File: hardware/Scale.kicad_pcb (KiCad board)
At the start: 2 copper layers, 58.2 x 25.9 mm, 45 parts, among them J1 Load Cell Connector, J2 DebugEdge_02x03, J3 Display Connector, J4 GPIO, J5 RS232, J6 USB_C_Receptacle, Q1 DMG2307L, Q2 DMG2307L, Q3 BSD235N, SW1 RESET, SW2 PEC12R Encoder, U1 STM32G070CBTx_u, U3 MCP6N11-010, U4 MCP4542, U5 AP9101CK, U6 MIC5504-3.3YM5, X1 KC2520Z

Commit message: Started on pcb
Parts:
- removed the C4 at (117.2, 60.7)
- removed J6: USB_C_Receptacle, Custom:USB_C_Receptacle_Amphenol_12401610E4-2A
- removed SW2: PEC12R Encoder, Custom:Bourns PEC12R Vertical
- added C10: 1uF, Capacitor_SMD:C_0603_1608Metric, F.Cu at (150.0, 63.8)
- added C12: 1uF, Capacitor_SMD:C_0603_1608Metric, F.Cu at (144.7, 66.0)
- added C13: 1uF, Capacitor_SMD:C_0603_1608Metric, F.Cu at (144.7, 64.5)
- added C14: 1uF, Capacitor_SMD:C_0603_1608Metric, F.Cu at (141.6, 66.0)
- added C15: 220nF, Capacitor_SMD:C_0603_1608Metric, F.Cu at (147.8, 67.5)
- added C16: 47nF, Capacitor_SMD:C_0603_1608Metric, F.Cu at (147.8, 70.6)
- added C18: 10uF, Capacitor_SMD:C_1210_3225Metric, F.Cu at (131.6, 58.8)
- added C19: 10uF, Capacitor_SMD:C_1210_3225Metric, F.Cu at (136.3, 56.0)
- added C23: 100nF, Capacitor_SMD:C_0603_1608Metric, F.Cu at (141.8, 69.6)
- added C27: 100nF, Capacitor_SMD:C_0603_1608Metric, F.Cu at (155.1, 47.7)
- added C28: 100nF, Capacitor_SMD:C_0603_1608Metric, F.Cu at (155.1, 49.2)
- added C29: 10uF, Capacitor_SMD:C_0603_1608Metric, F.Cu at (152.8, 48.4)
- added C30: 100nF, Capacitor_SMD:C_0603_1608Metric, F.Cu at (156.6, 59.1)
- added C31: 100nF, Capacitor_SMD:C_0603_1608Metric, F.Cu at (156.7, 60.6)
- added C5: 100nF, Capacitor_SMD:C_0603_1608Metric, F.Cu at (137.2, 69.5)
- added C6: 10nF, Capacitor_SMD:C_0603_1608Metric, F.Cu at (149.5, 53.9)
- added C7: 100nF, Capacitor_SMD:C_0603_1608Metric, F.Cu at (146.2, 51.9)
- added C8: 10nF, Capacitor_SMD:C_0603_1608Metric, F.Cu at (143.0, 53.9)
- added C9: 100nF, Capacitor_SMD:C_0603_1608Metric, F.Cu at (140.3, 69.6)
- added J7: 12401610E4#2A, custom:12401610E42A, F.Cu at (118.3, 52.9)
- added L1: 10uH, Inductor_SMD:L_1210_3225Metric, F.Cu at (139.7, 56.0)
- added R1: 1.0K 1%, Resistor_SMD:R_0603_1608Metric, F.Cu at (68.7, 48.3)
- added R10: 20k 1%, Resistor_SMD:R_0603_1608Metric, F.Cu at (143.8, 51.6)
- added R11: 20k 1%, Resistor_SMD:R_0603_1608Metric, F.Cu at (141.6, 64.5)
- added R13: 20k 1%, Resistor_SMD:R_0603_1608Metric, F.Cu at (147.0, 63.7)
- added R16: 20k 1%, Resistor_SMD:R_0603_1608Metric, F.Cu at (148.5, 63.8)
- added R17: 10k 1%, Resistor_SMD:R_0603_1608Metric, F.Cu at (147.8, 66.0)
- added R18: 20k 1%, Resistor_SMD:R_0603_1608Metric, F.Cu at (147.8, 69.1)
- added R2: 1.0K 1%, Resistor_SMD:R_0603_1608Metric, F.Cu at (68.7, 50.8)
- added R27: 1K, Resistor_SMD:R_0603_1608Metric, F.Cu at (68.7, 63.4)
- added R28: 1K, Resistor_SMD:R_0603_1608Metric, F.Cu at (68.7, 65.9)
- added R29: 1K, Resistor_SMD:R_0603_1608Metric, F.Cu at (68.7, 68.4)
- added R3: 1.0K 1%, Resistor_SMD:R_0603_1608Metric, F.Cu at (68.7, 53.3)
- added R36: 10R 1%, Resistor_SMD:R_0603_1608Metric, F.Cu at (157.3, 48.4)
- added R37: 10R 1%, Resistor_SMD:R_0603_1608Metric, F.Cu at (157.4, 62.8)
- added R38: 10R 1%, Resistor_SMD:R_0603_1608Metric, F.Cu at (155.9, 67.2)
- added R39: 10R 1%, Resistor_SMD:R_0603_1608Metric, F.Cu at (154.4, 67.2)
- added R4: 1.0K 1%, Resistor_SMD:R_0603_1608Metric, F.Cu at (68.7, 55.9)
- added R40: 10R 1%, Resistor_SMD:R_0603_1608Metric, F.Cu at (152.9, 67.2)
- added R41: 10R 1%, Resistor_SMD:R_0603_1608Metric, F.Cu at (151.4, 67.2)
- added R42: 10R 1%, Resistor_SMD:R_0603_1608Metric, F.Cu at (155.9, 62.9)
- added R43: 10R 1%, Resistor_SMD:R_0603_1608Metric, F.Cu at (154.4, 62.8)
- added R44: 10K 1%, Resistor_SMD:R_0603_1608Metric, F.Cu at (156.7, 65.0)
- added R5: 1.0K 1%, Resistor_SMD:R_0603_1608Metric, F.Cu at (68.7, 58.4)
- added R6: 1.0K 1%, Resistor_SMD:R_0603_1608Metric, F.Cu at (68.7, 60.9)
- added R7: 100k 1%, Resistor_SMD:R_0603_1608Metric, F.Cu at (138.2, 67.2)
- added R8: 100k 1%, Resistor_SMD:R_0603_1608Metric, F.Cu at (138.7, 69.5)
- added R9: 20k 1%, Resistor_SMD:R_0603_1608Metric, F.Cu at (148.8, 51.6)
- added S1: PEC12R-3217F-S0024, custom:PEC12R3217FS0024, F.Cu at (151.7, 89.7)
- added TP1: TP_INA_OUT_UNFILTERED, TestPoint:TestPoint_Pad_D1.5mm, B.Cu at (72.5, 48.8)
- added TP2: TP_ADC_VREF, TestPoint:TestPoint_Pad_D1.5mm, B.Cu at (72.5, 52.4)
- added TP3: TP_INA_OUT_ACTIVE, TestPoint:TestPoint_Pad_D1.5mm, B.Cu at (72.5, 55.9)
- added TP4: TP_INA_OUT_FILTERED_PASSIVE, TestPoint:TestPoint_Pad_D1.5mm, B.Cu at (72.5, 59.5)
- added TP5: TP_INA_IN_P, TestPoint:TestPoint_Pad_D1.5mm, B.Cu at (76.1, 48.8)
- added TP6: TP_INA_IN_N, TestPoint:TestPoint_Pad_D1.5mm, B.Cu at (76.1, 52.4)
- added TP_3V1: TP_3V3, TestPoint:TestPoint_Pad_D1.5mm, B.Cu at (76.1, 55.9)
- added TP_3V3A1: TP_3V3A, TestPoint:TestPoint_Pad_D1.5mm, B.Cu at (76.1, 59.5)
- added TP_BAT_N1: TP_BAT_N, TestPoint:TestPoint_Pad_D1.5mm, B.Cu at (79.6, 48.8)
- added TP_GND1: TP_GND, TestPoint:TestPoint_Pad_D1.5mm, B.Cu at (79.6, 52.4)
- added TP_VDD1: TP_VDD, TestPoint:TestPoint_Pad_D1.5mm, B.Cu at (79.6, 55.9)
- added U10: MCP6001-OT, Package_TO_SOT_SMD:SOT-23-5, F.Cu at (138.2, 64.3)
- added U2: MCP3562R-E/ST, Package_SO:TSSOP-20_4.4x6.5mm_P0.65mm, F.Cu at (154.7, 54.5)
- added U9: MCP6001-OT, Package_TO_SOT_SMD:SOT-23-5, F.Cu at (144.4, 69.0)
- C1, C2, C3: footprint Capacitor_SMD:C_0603_1608Metric_Pad1.08x0.95mm_HandSolder -> Capacitor_SMD:C_0603_1608Metric
- C11: renamed from C6; footprint Capacitor_SMD:C_0603_1608Metric_Pad1.08x0.95mm_HandSolder -> Capacitor_SMD:C_0603_1608Metric
- C17: renamed from C7; footprint Capacitor_SMD:C_0603_1608Metric_Pad1.08x0.95mm_HandSolder -> Capacitor_SMD:C_0603_1608Metric
- C4: renamed from C5; footprint Capacitor_SMD:C_0603_1608Metric_Pad1.08x0.95mm_HandSolder -> Capacitor_SMD:C_0603_1608Metric
- D1: footprint Diode_SMD:D_SOD-323_HandSoldering -> Diode_SMD:D_SOD-323F
- J4: renamed from J2; footprint custom:DebugEdge_2x03_Target -> Connector_DebugEdge:DebugEdge_2x03_Target
- J5: renamed from J3; footprint Custom:0.96'' Display -> Connector_PinHeader_2.54mm:PinHeader_1x04_P2.54mm_Vertical
- R12: renamed from R1; footprint Resistor_SMD:R_0603_1608Metric_Pad0.98x0.95mm_HandSolder -> Resistor_SMD:R_0603_1608Metric
- R14: renamed from R2; footprint Resistor_SMD:R_0603_1608Metric_Pad0.98x0.95mm_HandSolder -> Resistor_SMD:R_0603_1608Metric
- R15: renamed from R3; footprint Resistor_SMD:R_0603_1608Metric_Pad0.98x0.95mm_HandSolder -> Resistor_SMD:R_0603_1608Metric
- R19: renamed from R9; footprint Resistor_SMD:R_0603_1608Metric_Pad0.98x0.95mm_HandSolder -> Resistor_SMD:R_0603_1608Metric
- R20: renamed from R10; footprint Resistor_SMD:R_0603_1608Metric_Pad0.98x0.95mm_HandSolder -> Resistor_SMD:R_0603_1608Metric
- R21: renamed from R11; footprint Resistor_SMD:R_0603_1608Metric_Pad0.98x0.95mm_HandSolder -> Resistor_SMD:R_0603_1608Metric
- R22: renamed from R12; footprint Resistor_SMD:R_0603_1608Metric_Pad0.98x0.95mm_HandSolder -> Resistor_SMD:R_0603_1608Metric
- R23: renamed from R13; footprint Resistor_SMD:R_0603_1608Metric_Pad0.98x0.95mm_HandSolder -> Resistor_SMD:R_0603_1608Metric
- R24: renamed from R14; footprint Resistor_SMD:R_0603_1608Metric_Pad0.98x0.95mm_HandSolder -> Resistor_SMD:R_0603_1608Metric
- R25: renamed from R15; footprint Resistor_SMD:R_0603_1608Metric_Pad0.98x0.95mm_HandSolder -> Resistor_SMD:R_0603_1608Metric
- R26: renamed from R16; footprint Resistor_SMD:R_0603_1608Metric_Pad0.98x0.95mm_HandSolder -> Resistor_SMD:R_0603_1608Metric
- moved J3 45.5 mm to (114.6, 90.2), turned to 90 degrees
- moved R33 40.5 mm to (135.0, 87.3), turned to 180 degrees
- moved C21 38.5 mm to (135.0, 85.8), turned to 0 degrees
- moved R22 20.5 mm to (129.0, 85.9)
- moved Q1 20.1 mm to (131.5, 86.4), turned to -90 degrees
- moved J5 19.5 mm to (129.8, 90.2), turned to -90 degrees
- moved R32 19.2 mm to (138.1, 84.3)
- moved C20 19.2 mm to (138.1, 79.7)
- moved R30 19.2 mm to (138.1, 81.3)
- moved R31 19.2 mm to (138.1, 82.8)
- moved C22 19.2 mm to (138.1, 87.3)
- moved R34 19.2 mm to (138.1, 85.8)
- moved C11 19.0 mm to (150.0, 60.8), turned to 90 degrees
- moved R19 18.4 mm to (127.5, 85.9), turned to 90 degrees
- moved J4 16.8 mm to (113.2, 63.6)
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- renumbered C8 to C20, C10 to C21, C9 to C22, J4 to J2, J5 to J3, R4 to R30, R5 to R31, R6 to R32, R7 to R33, R8 to R34, U5 to U7, U6 to U8
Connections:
- net /I2C_SCL renamed /Display/SCL
- net /I2C_SDA renamed /Display/SDA
- net /Instrumentation Amplifier/INA_OUT renamed /Instrumentation Amplifier/INA_OUT_UNFILTERED
- C11 pad 1: +3V3 -> +3.3VA
- C3 pad 1: /MCU/MCU_VREF -> +3.3VA
- D1 pad 1: /Instrumentation Amplifier/BRIDGE_B -> /Instrumentation Amplifier/INA_IN_P
- D1 pad 2: /Instrumentation Amplifier/BRIDGE_A -> /Instrumentation Amplifier/INA_IN_N
- J2 pad 1: /MCU/GPIO_PA5 -> /MCU/GPIO_PB7
- Q2 pad 2: +3V3 -> +3.3VA
- R23 pad 1: +3V3 -> +3.3VA
- R25 pad 1: +BATT -> /MCU/LDO_EN
- R25 pad 2: Net-(R15-Pad2) -> GND
- U1 pad 1: unconnected-(U1-Pad1) -> /ADC/ADC_IRQ
- U1 pad 11: /Encoder/ENCODER_BUTTON -> /ADC/ADC_VREF
- U1 pad 13: /MCU/DISPLAY_ENABLE -> /Instrumentation Amplifier/INA_OUT_FILTERED_PASSIVE
- U1 pad 14: /MCU/BRIDGE_ENABLE -> /ADC/INA_OUT_FILTERED_ACTIVE
- U1 pad 15: /Instrumentation Amplifier/DPOT_HVC_A0 -> unconnected-(U1A-PA4/ADC1_IN4/I2S1_WS/RTC_OUT_ALARM/RTC_OUT_CALIB/SPI1_NSS/SPI2_MOSI/TIM14_CH1-Pad15)
- U1 pad 16: /MCU/GPIO_PA5 -> /Encoder/ENCODER_BUTTON
- U1 pad 22: unconnected-(U1-Pad22) -> /MCU/DISPLAY_ENABLE
- U1 pad 23: unconnected-(U1-Pad23) -> /MCU/BRIDGE_ENABLE
- U1 pad 24: unconnected-(U1-Pad24) -> /ADC/~{SS}
- U1 pad 25: unconnected-(U1-Pad25) -> /ADC/CLK
- U1 pad 26: unconnected-(U1-Pad26) -> /ADC/MISO
- U1 pad 27: unconnected-(U1-Pad27) -> /ADC/MOSI
- U1 pad 3: unconnected-(U1-Pad3) -> /MCU/LDO_EN
- U1 pad 4: +3V3 -> +BATT
- U1 pad 40: unconnected-(U1-Pad40) -> /ADC/ADC_MCLK
- U1 pad 41: unconnected-(U1-Pad41) -> /Instrumentation Amplifier/DPOT_HVC_A0
- U1 pad 45: /MCU/USART_TX -> /MCU/GPIO_PB5
- U1 pad 46: /MCU/USART_RX -> /MCU/GPIO_PB7
- U1 pad 47: unconnected-(U1-Pad47) -> /MCU/USART_TX
- U1 pad 48: unconnected-(U1-Pad48) -> /MCU/USART_RX
- U1 pad 5: /MCU/MCU_VREF -> +3.3VA
- U3 pad 2: /Instrumentation Amplifier/BRIDGE_A -> /Instrumentation Amplifier/INA_IN_N
- U3 pad 3: /Instrumentation Amplifier/BRIDGE_B -> /Instrumentation Amplifier/INA_IN_P
- U3 pad 5: GND -> /Instrumentation Amplifier/INA_VREF
- U3 pad 7: +3V3 -> +3.3VA
- U4 pad 5: GND -> /Instrumentation Amplifier/INA_VREF
- U8 pad 3: Net-(R15-Pad2) -> /MCU/LDO_EN
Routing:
- net +3V3: track 102.3 -> 13.8 mm, vias 2 -> 0
- net /MCU/SWDIO: track 33.7 -> 0.00 mm, vias 2 -> 0
- net +3.3VA: track 0.00 -> 33.7 mm
- net /MCU/SWDCLK: track 33.3 -> 0.00 mm, vias 3 -> 0
- net /MCU/GPIO_PA8: track 30.4 -> 0.00 mm, vias 2 -> 0
- net /Encoder/ENCODER_BUTTON: track 44.6 -> 14.4 mm, vias 4 -> 0
- net /ADC/INA_OUT_FILTERED_ACTIVE: track 0.00 -> 29.8 mm
- net /Instrumentation Amplifier/INA_OUT_UNFILTERED: track 31.7 -> 5.83 mm
- net /MCU/GPIO_PA5: track 24.0 -> 0.00 mm
- net /MCU/DISPLAY_ENABLE: track 23.7 -> 0.00 mm, vias 2 -> 0
- net /MCU/USART_RTS: track 22.7 -> 0.00 mm, vias 2 -> 0
- net /MCU/GPIO_PB3: track 21.8 -> 0.00 mm, vias 1 -> 0
- net /MCU/GPIO_PB0: track 21.8 -> 0.00 mm
- net /Instrumentation Amplifier/INA_IN_P: track 0.00 -> 21.7 mm
- net /ADC/ADC_VREF: track 0.00 -> 19.9 mm
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- removed copper zone on B.Cu, net GND
- removed copper zone on F.Cu, net GND
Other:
- board size 58.2 x 25.9 mm -> 45 x 45 mm

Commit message: Added solder bridges and calculated resistor values for INA
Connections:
- U1 pad 39: unconnected-(U1D-PD1/SPI2_SCK/TIM17_CH1-Pad39) -> /ADC/ADC_MCLK
- U1 pad 40: /ADC/ADC_MCLK -> unconnected-(U1D-PD2/TIM1_CH1N/TIM3_ETR/USART3_CK/USART3_DE/USART3_RTS-Pad40)
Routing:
- net Net-(U2-SDI): track 10.3 -> 0.00 mm
- net Net-(U2-*CS): track 9.24 -> 0.00 mm
- net Net-(U2-SCK): track 8.89 -> 0.00 mm
- net /ADC/ADC_MCLK: track 6.61 -> 0.00 mm

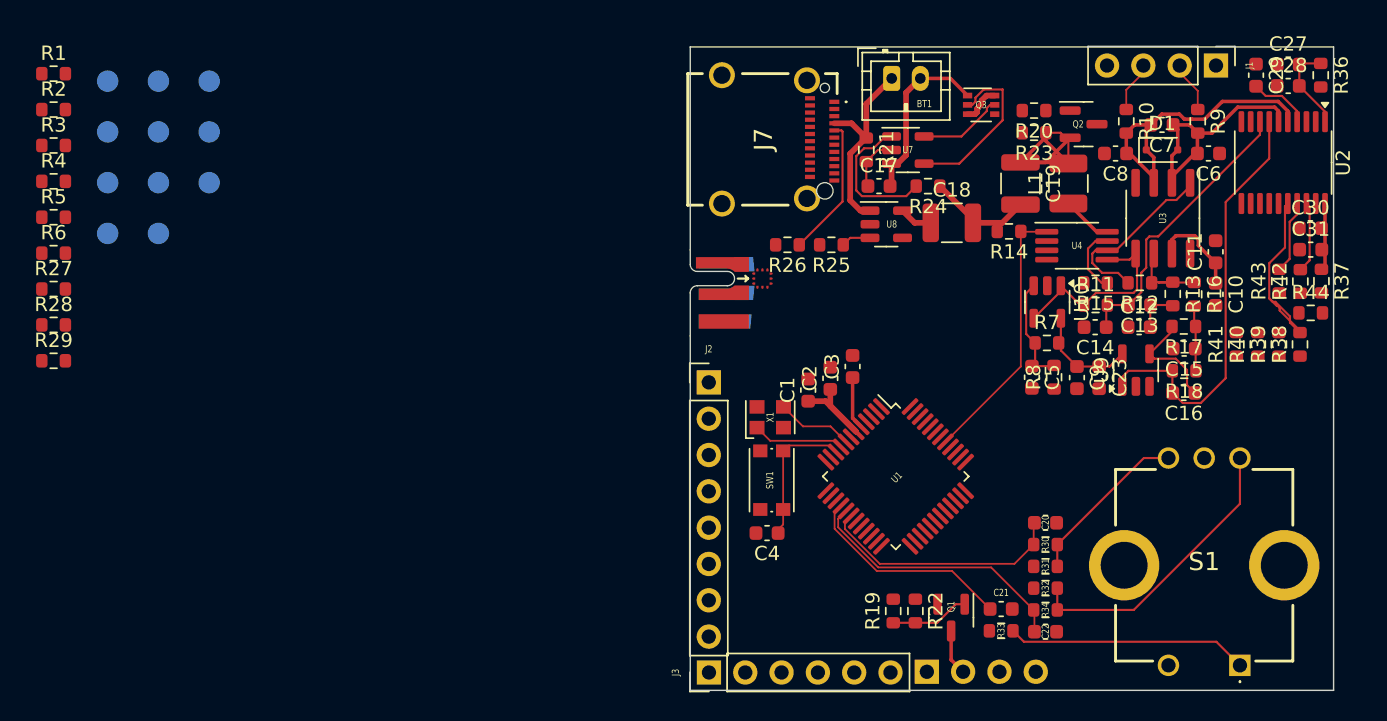
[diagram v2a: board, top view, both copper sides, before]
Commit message: Set jumper footprints and updated design rules for Oshpark After Dark
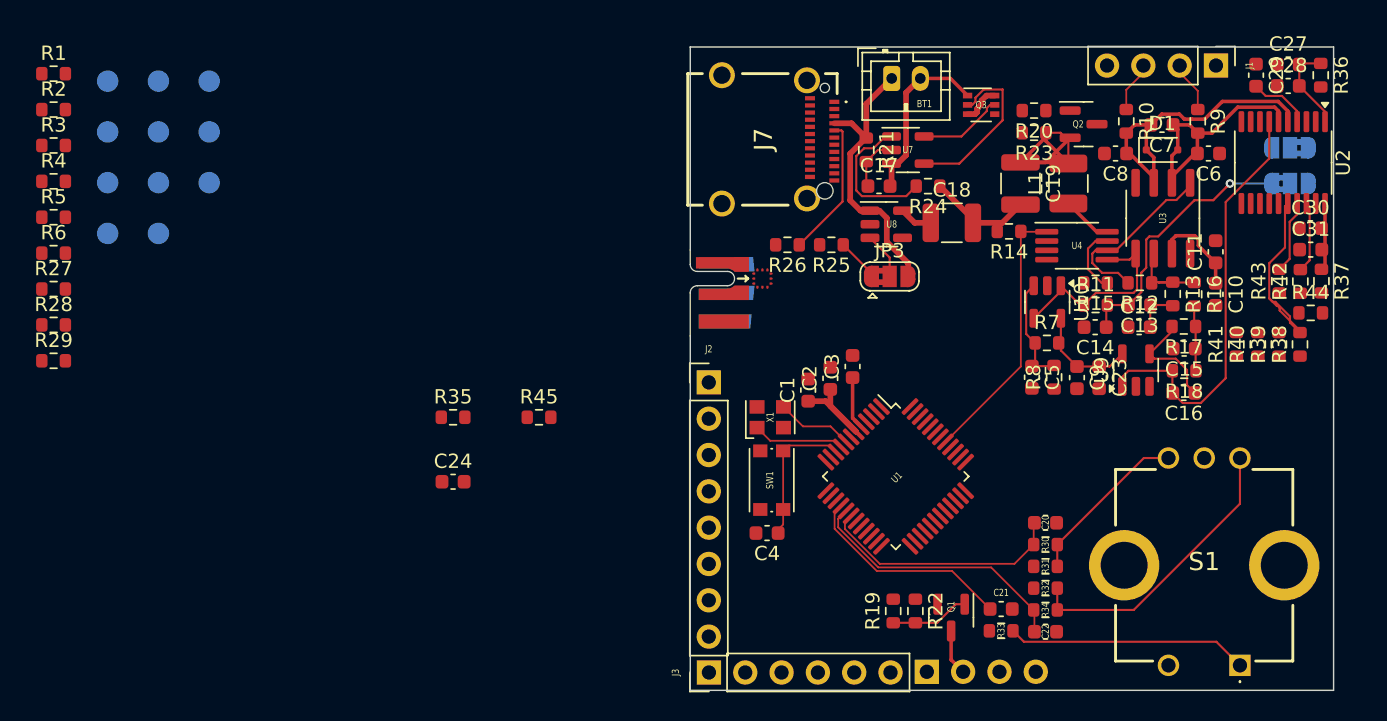
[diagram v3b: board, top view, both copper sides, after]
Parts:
- added C24: 1uF, Capacitor_SMD:C_0603_1608Metric, F.Cu at (96.7, 76.9)
- added JP1: SolderJumper_3_Bridged12, Jumper:SolderJumper-3_P1.3mm_Bridged2Bar12_RoundedPad1.0x1.5mm, B.Cu at (155.2, 56.0)
- added JP2: SolderJumper_3_Bridged12, Jumper:SolderJumper-3_P1.3mm_Bridged2Bar12_RoundedPad1.0x1.5mm, B.Cu at (155.2, 53.5)
- added JP3: SolderJumper_3_Bridged12, Jumper:SolderJumper-3_P1.3mm_Bridged2Bar12_RoundedPad1.0x1.5mm, F.Cu at (127.2, 62.5)
- added R35: 10K 1%, Resistor_SMD:R_0603_1608Metric, F.Cu at (96.7, 72.3)
- added R45: 1k 1%, Resistor_SMD:R_0603_1608Metric, F.Cu at (102.7, 72.3)
- R12: value 100k 1% -> 330k 1%
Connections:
- U2 pad 3: GND -> Net-(JP1-C)
- U2 pad 8: /ADC/ADC_VREF -> /ADC/INA_OUT_FILTERED_PASSIVE
- U4 pad 5: /Instrumentation Amplifier/INA_VREF -> Net-(U4-P0W)
- U8 pad 3: /MCU/LDO_EN -> Net-(JP3-C)
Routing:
- net +BATT: track 14.1 -> 20.2 mm
- net Net-(JP3-C): track 0.00 -> 2.97 mm
- net /ADC/ADC_VREF: track 19.9 -> 18.8 mm, vias 0 -> 1
- net /MCU/LDO_EN: track 2.08 -> 3.02 mm

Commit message: Some more routing
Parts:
- removed JP3: SolderJumper_3_Bridged12, Jumper:SolderJumper-3_P1.3mm_Bridged2Bar12_RoundedPad1.0x1.5mm
- removed R25: 100K, Resistor_SMD:R_0603_1608Metric
- moved R35 56.0 mm to (151.4, 60.8), turned to -90 degrees
- moved R45 42.7 mm to (142.5, 57.0), turned to -90 degrees
- moved C24 31.3 mm to (123.2, 60.3)
- moved R40 5.10 mm to (152.9, 72.3), turned to 180 degrees
- moved R41 3.90 mm to (152.9, 70.8), turned to 180 degrees
- turned C14 to 0 degrees
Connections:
- U1 pad 3: /MCU/LDO_EN -> unconnected-(U1C-PC15-OSC32_OUT(PC15)/RCC_OSC32_EN/RCC_OSC32_OUT/RCC_OSC_EN/TIM15_BK-Pad3)
- U1 pad 4: +BATT -> +3.3VA
- U8 pad 3: Net-(JP3-C) -> +BATT
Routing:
- net /ADC/ADC_IRQ: track 0.00 -> 38.1 mm, vias 0 -> 4
- net /MCU/BRIDGE_ENABLE: track 0.00 -> 36.1 mm
- net /ADC/~{SS}: track 0.00 -> 34.4 mm
- net /ADC/MISO: track 0.00 -> 34.3 mm
- net /ADC/ADC_MCLK: track 0.00 -> 33.3 mm, vias 0 -> 4
- net /ADC/MOSI: track 0.00 -> 32.6 mm
- net /Instrumentation Amplifier/INA_ENABLE: track 0.00 -> 32.3 mm, vias 0 -> 4
- net /ADC/CLK: track 0.00 -> 29.6 mm
- net /Instrumentation Amplifier/INA_OUT_FILTERED_PASSIVE: track 3.03 -> 31.7 mm, vias 0 -> 2
- net /ADC/INA_OUT_FILTERED_ACTIVE: track 29.8 -> 57.8 mm, vias 0 -> 2
- net /MCU/GPIO_PA8: track 0.00 -> 18.5 mm, vias 0 -> 2
- net /MCU/GPIO_PB0: track 0.00 -> 16.6 mm
- net Net-(U2-SCK): track 0.00 -> 16.2 mm
- net /MCU/GPIO_PB1: track 0.00 -> 15.3 mm
- net /Display/SDA: track 0.00 -> 14.4 mm, vias 0 -> 2
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- added copper zone on B.Cu, net GND
- added copper zone on F.Cu, net GND

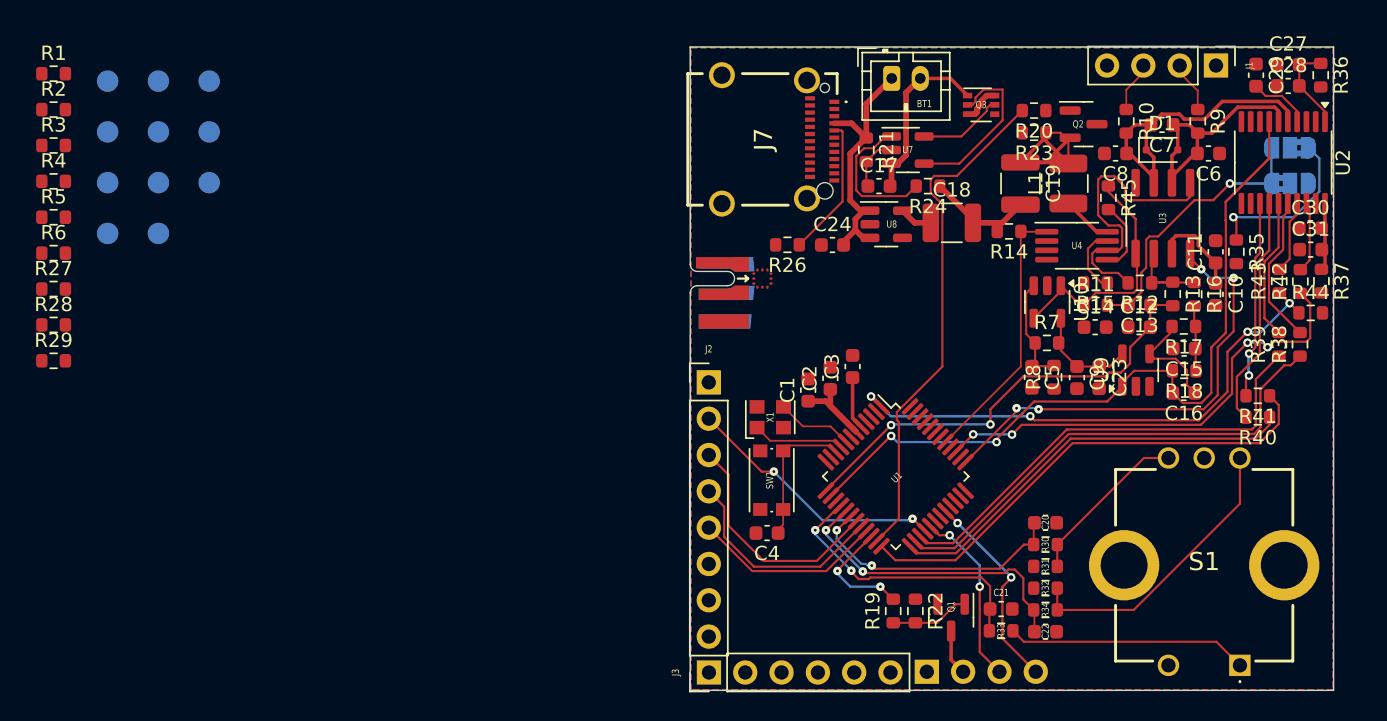
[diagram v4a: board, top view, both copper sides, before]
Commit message: Updated design rules and ran and implemented DRC
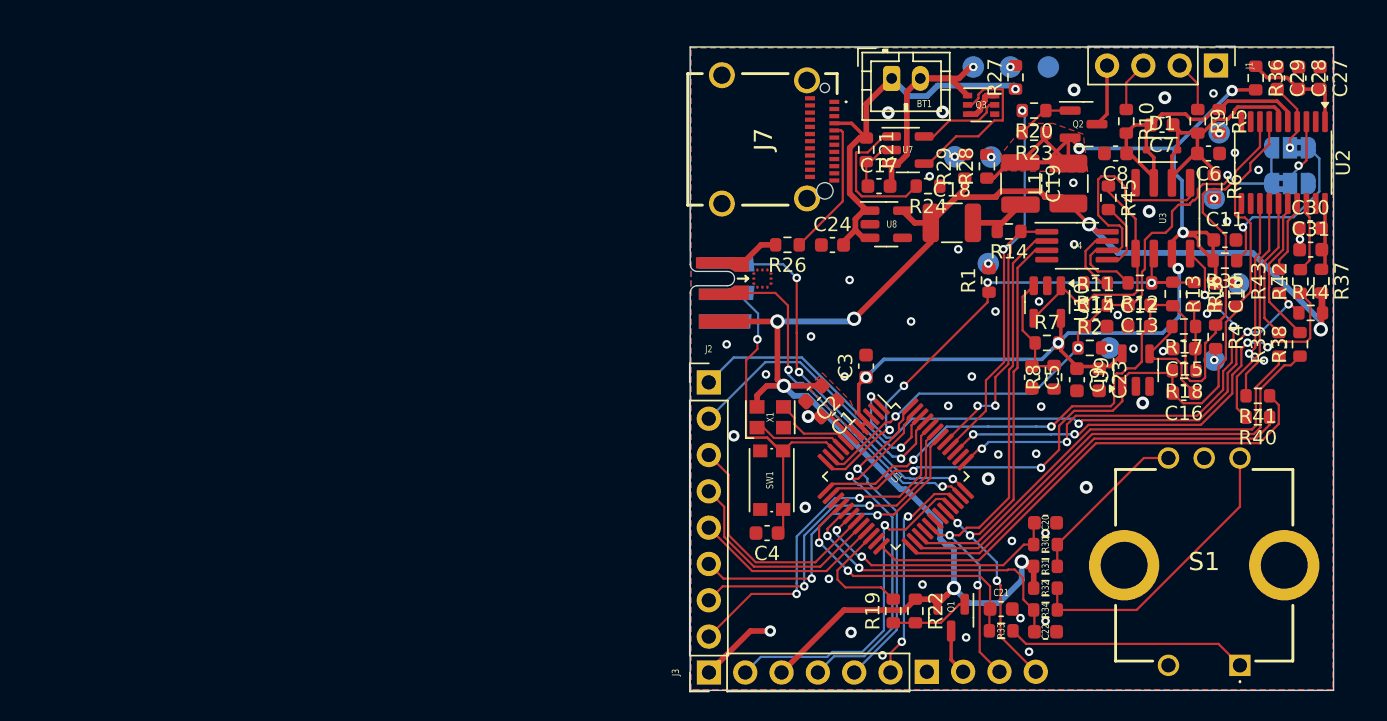
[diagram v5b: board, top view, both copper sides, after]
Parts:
- moved R3 83.4 mm to (151.4, 63.8), turned to 90 degrees
- moved R4 82.0 mm to (150.0, 66.7), turned to -90 degrees
- moved R5 81.8 mm to (150.2, 51.6), turned to -90 degrees
- moved R6 81.3 mm to (149.9, 56.2), turned to -90 degrees
- moved TP3 79.4 mm to (151.6, 63.0), turned to -90 degrees
- moved TP4 77.9 mm to (149.9, 68.3)
- moved R2 74.4 mm to (141.2, 67.5)
- moved TP5 74.3 mm to (150.2, 52.5)
- moved TP6 74.0 mm to (149.9, 57.0)
- moved TP2 71.7 mm to (142.6, 67.5)
- moved R27 68.9 mm to (136.0, 48.6), turned to 90 degrees
- moved R1 67.0 mm to (134.2, 62.8), turned to 90 degrees
- moved R28 66.2 mm to (134.0, 54.8), turned to 90 degrees
- moved R29 65.2 mm to (132.4, 54.8), turned to 90 degrees
- moved TP1 62.9 mm to (134.1, 61.6), turned to -90 degrees
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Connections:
- C12 pad 2: /Instrumentation Amplifier/INA_OUT_FILTERED_PASSIVE -> /ADC/INA_OUT_FILTERED_PASSIVE
- C13 pad 1: /Instrumentation Amplifier/INA_OUT_FILTERED_PASSIVE -> /ADC/INA_OUT_FILTERED_PASSIVE
- J2 pad 2: /MCU/GPIO_PA8 -> /MCU/GPIO_PB6
- J4 pad 6: /MCU/SWO -> unconnected-(J4-SWO/TDO-Pad6)
- R13 pad 2: /Instrumentation Amplifier/INA_OUT_FILTERED_PASSIVE -> /ADC/INA_OUT_FILTERED_PASSIVE
- R4 pad 1: /Instrumentation Amplifier/INA_OUT_FILTERED_PASSIVE -> /ADC/INA_OUT_FILTERED_PASSIVE
- U1 pad 13: /Instrumentation Amplifier/INA_OUT_FILTERED_PASSIVE -> /ADC/INA_OUT_FILTERED_PASSIVE
- U1 pad 23: /MCU/BRIDGE_ENABLE -> unconnected-(U1B-PB11/ADC1_EXTI11/ADC1_IN15/I2C2_SDA/SPI2_MOSI/USART3_RX-Pad23)
- U1 pad 28: /MCU/GPIO_PA8 -> unconnected-(U1A-PA8/RCC_MCO/SPI2_NSS/TIM1_CH1-Pad28)
- U1 pad 40: unconnected-(U1D-PD2/TIM1_CH1N/TIM3_ETR/USART3_CK/USART3_DE/USART3_RTS-Pad40) -> /MCU/BRIDGE_ENABLE
- U1 pad 45: /MCU/GPIO_PB5 -> /MCU/GPIO_PB6
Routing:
- net +3V3: track 13.8 -> 115.1 mm, vias 0 -> 7
- net /ADC/INA_OUT_FILTERED_PASSIVE: track 0.00 -> 62.1 mm, vias 0 -> 2
- net +3.3VA: track 33.7 -> 86.6 mm, vias 0 -> 6
- net /Instrumentation Amplifier/INA_OUT_FILTERED_PASSIVE: track 31.7 -> 0.00 mm, vias 2 -> 0
- net /Instrumentation Amplifier/INA_OUT_UNFILTERED: track 5.83 -> 37.6 mm, vias 0 -> 4
- net /MCU/SWDCLK: track 0.00 -> 27.5 mm, vias 0 -> 3
- net /ADC/ADC_VREF: track 19.4 -> 46.8 mm, vias 1 -> 3
- net /MCU/GPIO_PB5: track 0.00 -> 25.5 mm, vias 0 -> 2
- net /MCU/USART_TX: track 0.00 -> 25.5 mm, vias 0 -> 1
- net /Display/SCL: track 12.6 -> 37.5 mm
- net /MCU/GPIO_PB4: track 0.00 -> 24.3 mm, vias 0 -> 2
- net /MCU/GPIO_PB3: track 0.00 -> 24.1 mm, vias 0 -> 2
- net /MCU/USART_CTS: track 0.00 -> 24.1 mm, vias 0 -> 1
- net /MCU/SWDIO: track 0.00 -> 24.0 mm, vias 0 -> 2
- net /MCU/USART_RX: track 0.00 -> 22.7 mm, vias 0 -> 1
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- added copper zone on F.Cu, net +3.3VA
- added copper zone on F.Cu, net +3V3
